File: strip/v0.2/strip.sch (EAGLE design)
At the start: 102 parts, among them IC1 LP2992, IC2 ADP3110A-SO8, IC3 MAX3051, IC4 OPA335, IC5 ADP3110A-SO8, IC6 ADP3110A-SO8, IC7 STM32F050CX, Q1 IRF7828, Q2 IRF7828, Q3 IRF7828, Q4 IRF7828, Q5 IRF7828, Q6 IRF7828

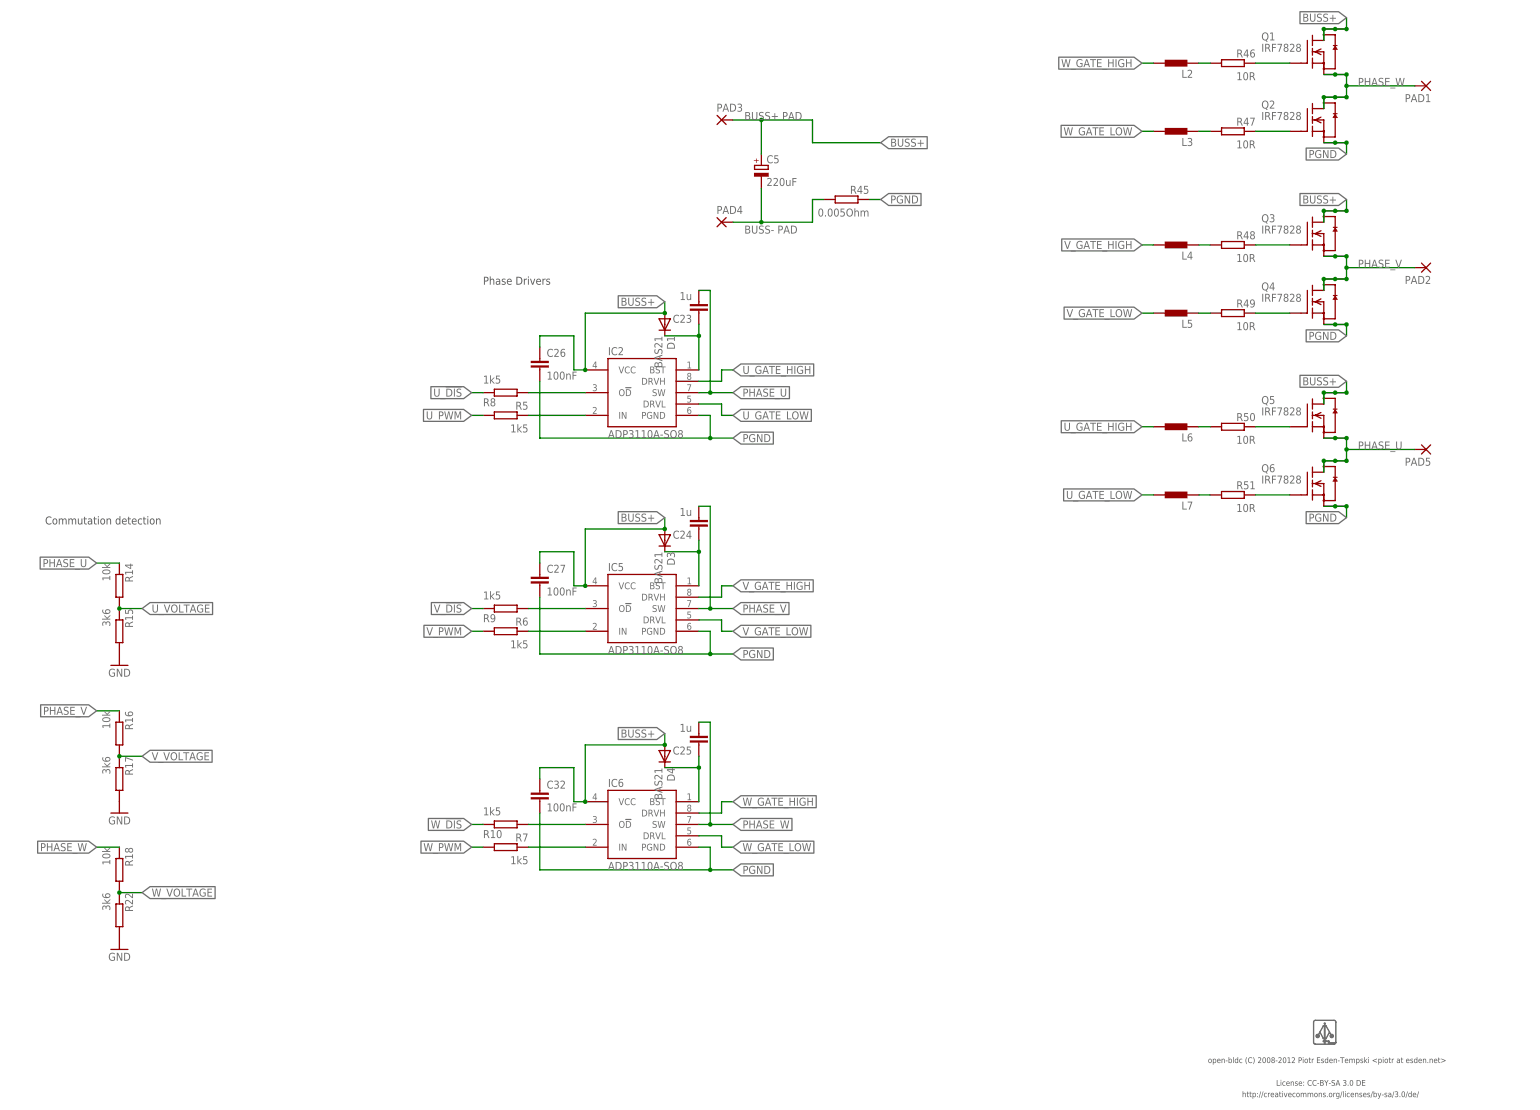
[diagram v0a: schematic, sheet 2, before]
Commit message: Added new variant of the strip board.
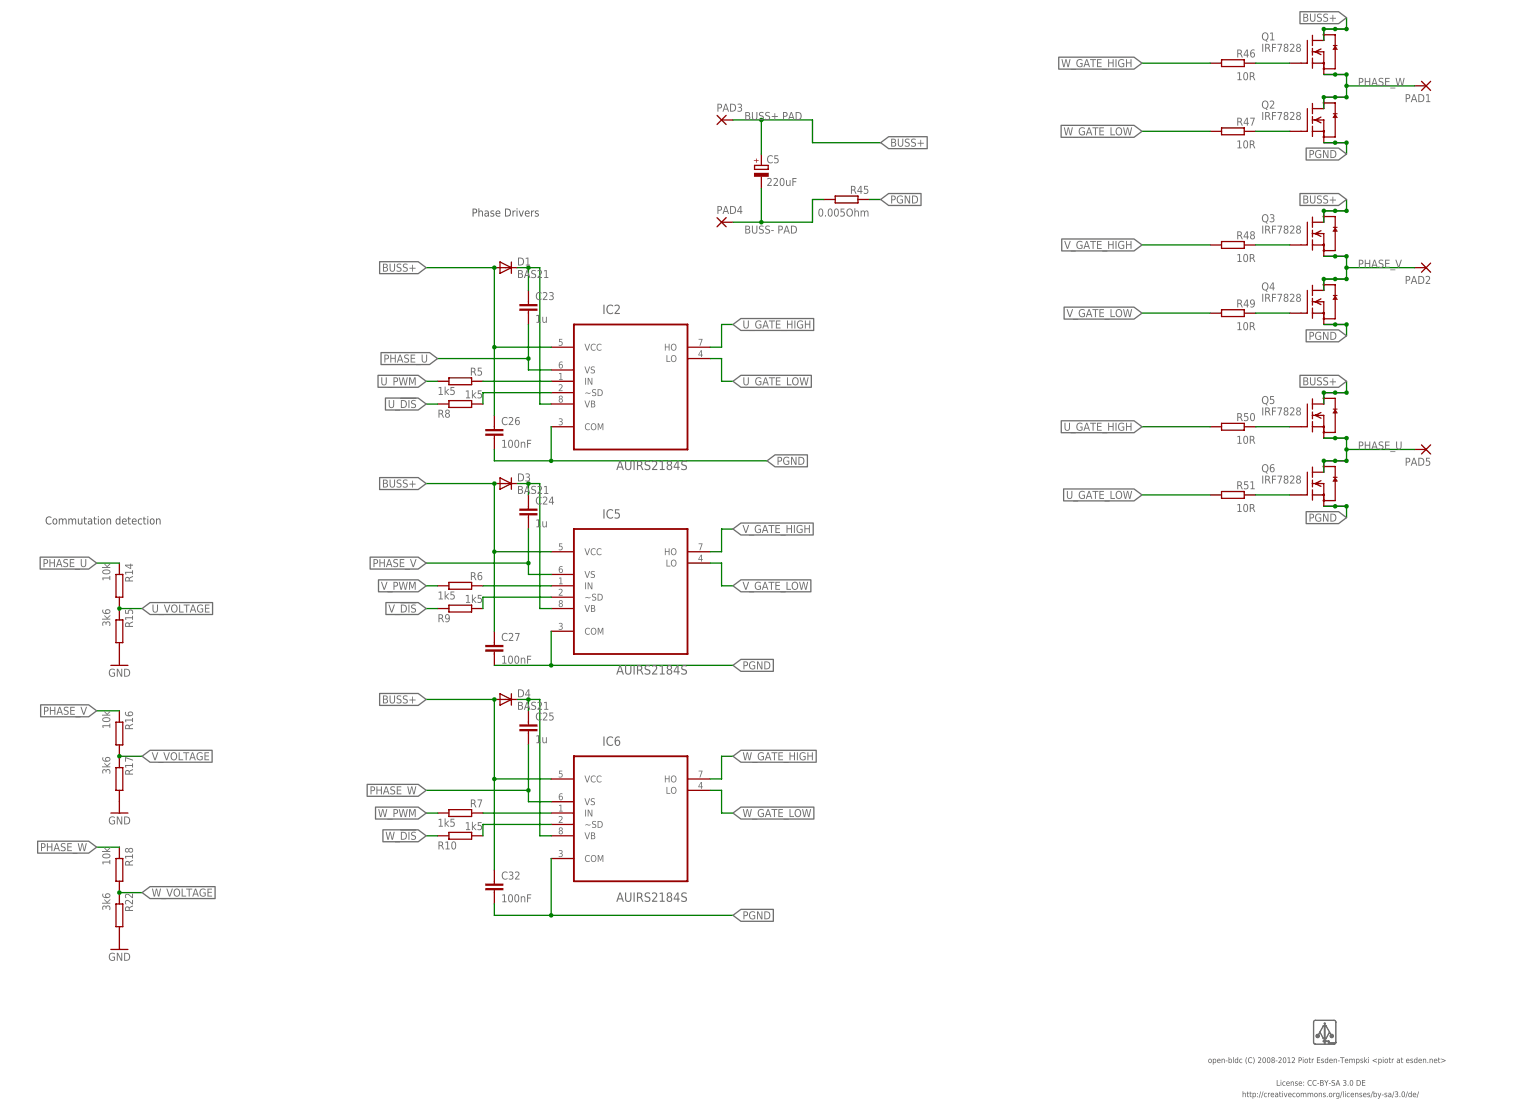
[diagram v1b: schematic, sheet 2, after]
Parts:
- removed L2, L3, L4, L5, L6, L7: (no value), pel_dipol_comp:INDUCTOR-0402
- C13: value 100nF -> 100n
- C26, C27, C32: device pel_dipol_comp:CAPACITOR-0402 -> pel_dipol_comp:CAPACITOR-0603
- D1, D3, D4: PARTNO diode-sod-123 -> *
- IC2, IC5, IC6: value ADP3110A-SO8 -> AUIRS2184S; device open-bldc:ADP3110A-SO8 -> auris2184s:AUIRS2184S
- IC3: PARTNO ic-so8-can-3v3 -> *
- IC7: PARTNO mcu-lqfp-48-stm32f05 -> mcu-tqfp-32-stm32f05
- R15, R17, R22: PARTNO res-0402-3k6 -> *
- R46, R47, R48, R49, R50, R51: device pel_dipol_comp:RESISTOR-0402 -> pel_dipol_comp:RESISTOR-0603
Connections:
- net N$29 renamed W_GATE_HIGH_T
- net N$30 renamed W_GATE_LOW_T
- net N$31 renamed V_GATE_HIGH_T
- net N$32 renamed V_GATE_LOW_T
- net N$34 renamed U_GATE_HIGH_T
- net N$35 renamed U_GATE_LOW_T
- net U_PWM1 renamed U_PWM_IN
- net V_PWM1 renamed V_PWM_IN
- net W_PWM1 renamed W_PWM_IN
- removed net N$2: C23.1, D1.C, IC2.BST
- removed net N$23: L2.2, R46.2
- removed net N$24: L3.2, R47.2
- removed net N$25: L4.2, R48.2
- removed net N$26: L5.2, R49.2
- removed net N$27: L6.2, R50.2
- removed net N$28: L7.2, R51.2
- removed net N$7: C24.1, D3.C, IC5.BST
- removed net N$8: C25.1, D4.C, IC6.BST
- removed net U_!DIS!1: IC2.O!D, R8.2
- removed net V_!DIS!1: IC5.O!D, R9.2
- removed net W_!DIS1: IC6.O!D, R10.2
- new net U_SD: IC2.~SD, R8.2
- new net U_VB: C23.1, D1.C, IC2.VB
- new net V_SD: IC5.~SD, R9.2
- new net V_VB: C24.1, D3.C, IC5.VB
- new net W_SD: IC6.~SD, R10.2
- new net W_VB: C25.1, D4.C, IC6.VB
- net PGND: no longer IC2.PGND, IC5.PGND, IC6.PGND
- net PHASE_U: now also IC2.VS; no longer IC2.SW
- net PHASE_V: now also IC5.VS; no longer IC5.SW
- net PHASE_W: now also IC6.VS; no longer IC6.SW
- net U_GATE_HIGH: now also IC2.HO, R50.2; no longer IC2.DRVH, L6.1
- net U_GATE_LOW: now also IC2.LO, R51.2; no longer IC2.DRVL, L7.1
- net V_GATE_HIGH: now also IC5.HO, R48.2; no longer IC5.DRVH, L4.1
- net V_GATE_LOW: now also IC5.LO, R49.2; no longer IC5.DRVL, L5.1
- net W_GATE_HIGH: now also IC6.HO, R46.2; no longer IC6.DRVH, L2.1
- net W_GATE_LOW: now also IC6.LO, R47.2; no longer IC6.DRVL, L3.1
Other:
- moved on the sheet: C23, C24, C25, C26, C27, C32, D1, D3, D4, R10, R5, R6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
